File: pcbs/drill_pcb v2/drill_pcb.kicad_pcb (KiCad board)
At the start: 2 copper layers, 105 x 103 mm, 49 parts, among them J1 24V IN, J10 LIMIT SWITCH BOTTOM, J11 DEEP WEIGHT SENSOR, J12 SURFACE WEIGHT SENSOR, J13 SERVO 1, J14 SERVO 2, J15 STEPPER STORAGE, J16 TEST PADS, J2 uC COMMUNICATION, J3 ENCODER VERTICAL DRIVE, J4 LIMIT SWITCH TOP, J5 HEIGHT SENSOR, J6 STEPPER VERTICAL DRIVE, J7 DC MOTOR 24 V, J8 DC MOTOR UART, J9 ENCODER STORAGE, Q3 SI2333-TP, U1 ESP32-DevKitC, U2 LM3940, U3 INA219BxD

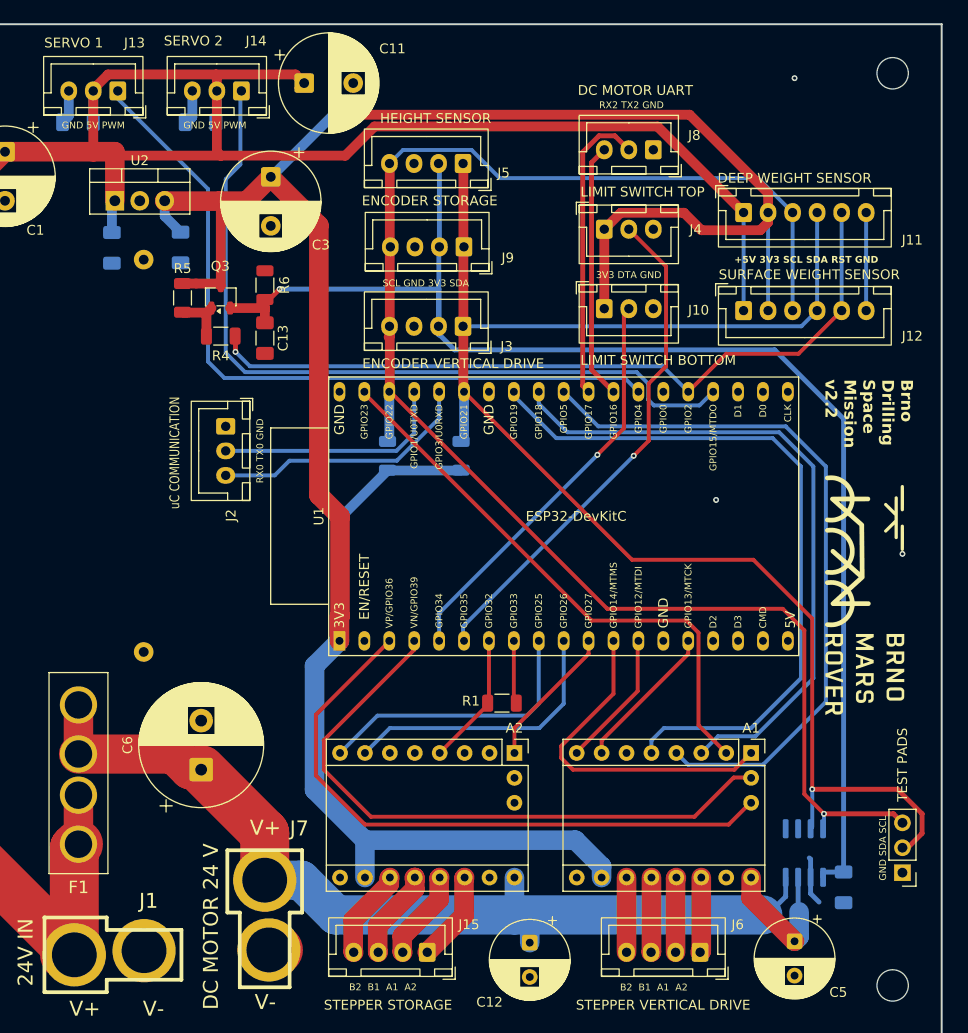
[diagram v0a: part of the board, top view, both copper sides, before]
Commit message: Last attempt at manufacturing did not work. Adjusted clearances.
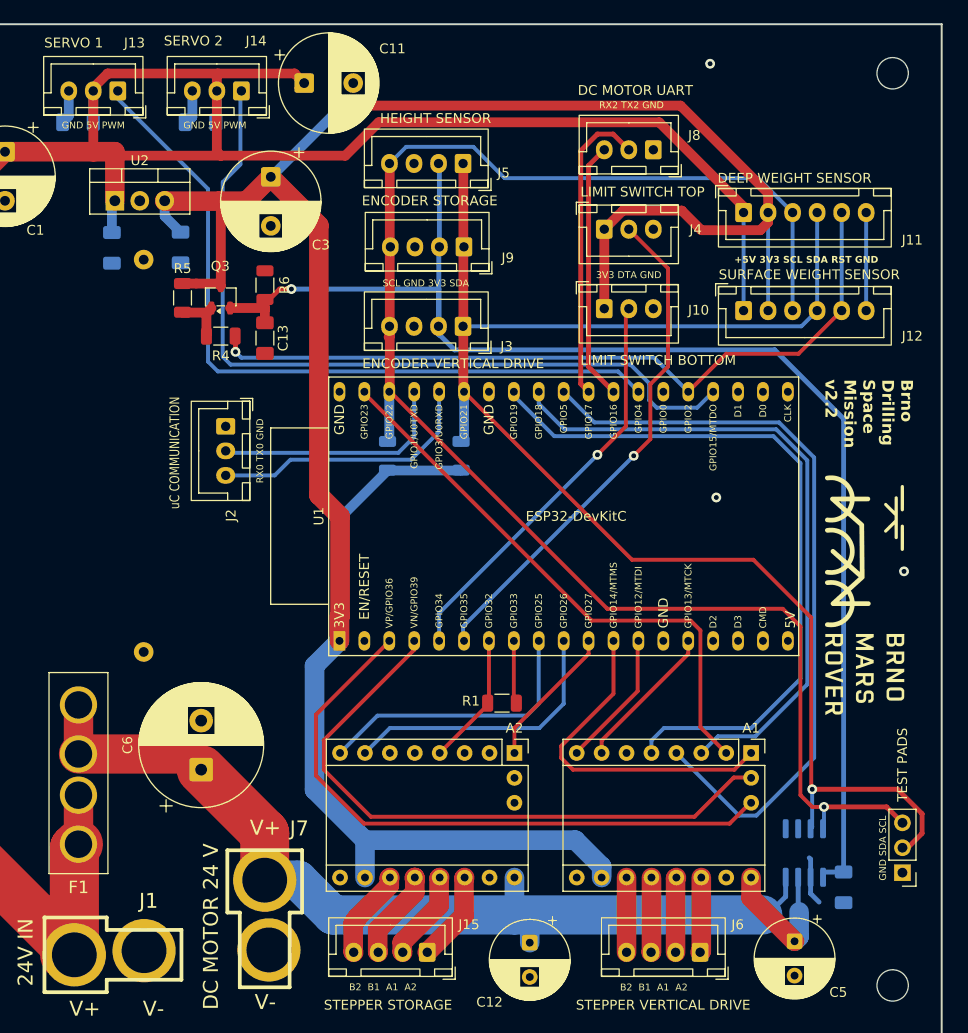
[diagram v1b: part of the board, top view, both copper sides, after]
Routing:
- net VSPI_CS1: track 72.3 -> 78.1 mm
- net SCL1: track 165.2 -> 166.4 mm
- net GND: track 23.7 -> 22.7 mm
- net +3.3V: track 255.6 -> 256.6 mm
- net SERVO2_PWM: track 80.8 -> 81.7 mm
- net +5V: track 155.8 -> 156.6 mm
- net RX0: track 26.9 -> 27.7 mm
- net VSPI_SCK: track 68.0 -> 67.5 mm
- net TX2: track 30.7 -> 31.2 mm
